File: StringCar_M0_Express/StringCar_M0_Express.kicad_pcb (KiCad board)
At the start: 2 copper layers, 50.8 x 22.9 mm, 48 parts, among them J1 USB_MICRO, J2 SENSOR_IN, J3 SWD, J4 STEMMA-QT, J5 MOTOR, J6 LIPO_BATT, Q1 DMG2305UX-13, Q2 DMG2305UX-13, SW1 RESET, SW2 POWER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

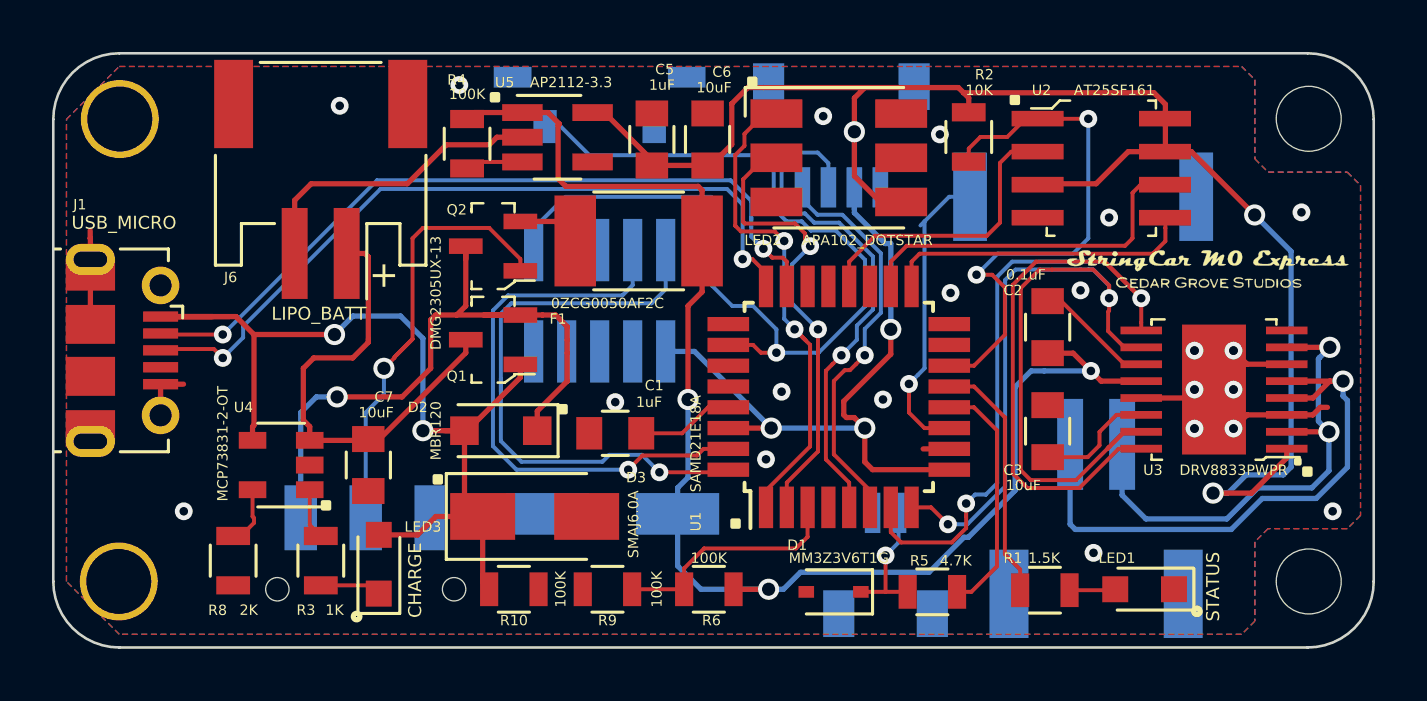
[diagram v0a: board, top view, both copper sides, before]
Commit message: update pcb layout and logo graphics
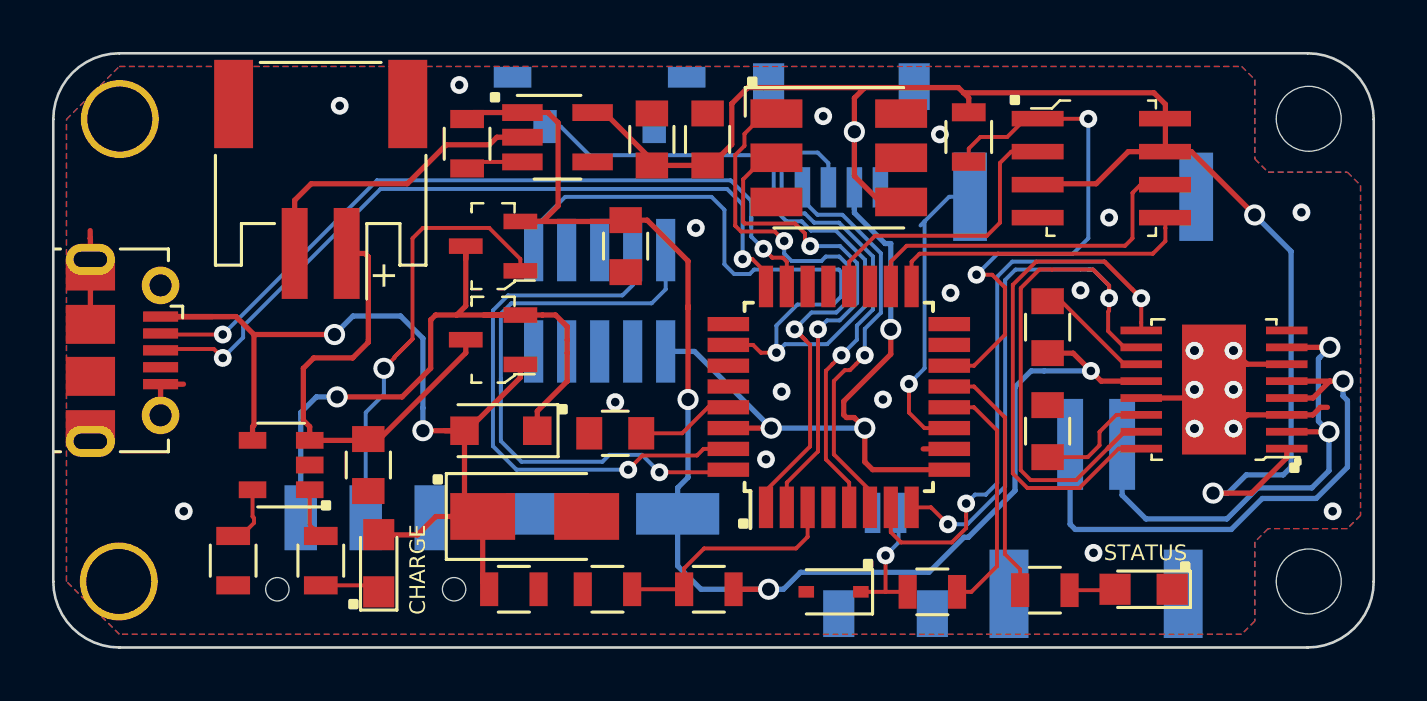
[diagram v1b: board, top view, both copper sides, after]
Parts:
- removed F1: 0ZCG0050AF2C, Resistors_SMD:R_1812
- removed the G*** at (138.4, 102.3)
- removed the G*** at (104.7, 97.0)
- removed the G*** at (105.3, 106.8)
- removed the G*** at (123.7, 103.1)
- removed the G*** at (124.3, 108.3)
- added C8: 0.01uF, Capacitors_SMD:C_0805, F.Cu at (116.0, 101.4)
- added G***: LOGO, Adafruit:stringcar_m0_express_6_5mmx2_8mm, B.Cu at (102.6, 97.6)
- added G***: LOGO, Adafruit:Blinka_3mmx3mm, F.Cu at (116.1, 105.3)
- added G***: LOGO, Adafruit:stringcar_m0_express_6_5mmx2_8mm, F.Cu at (140.5, 102.2)
- added G***: LOGO, Adafruit:Blinka_3mmx3mm, B.Cu at (98.2, 99.8)
- LED1, LED3: footprint Adafruit:D_0805_hand_soldering -> LEDs:LED_0805
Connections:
- Q2 pad 2: /Vsw -> /V+
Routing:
- net /~RESET: track 39.0 -> 44.1 mm
- net /DOTSTAR_DI: track 19.3 -> 22.9 mm
- net /Vsw: track 2.42 -> 0.00 mm
- net /DOTSTAR_CI: track 17.6 -> 19.2 mm
- net /V+: track 54.0 -> 55.3 mm
- net GND: vias 21 -> 22
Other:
- board text added: "--GND--"
- board text added: "2019-10-20 v04"
- board text added: "3V"
- board text added: "C"
- board text added: "D"
- board text added: "G 3V SDA SCL"
- board text added: "~R"
- board text removed: "+ CircuitPython compatible + AT-SAMD21E18A MPU + 2MByte flash RAM + Dual H-bridge motor controller + Sensor input + Stemma-QT connector (3V3) + On-board LiPo mgt 0.5A charge rate"
- board text removed: "2019-10-02 v03"
- board text removed: "3V3"
- board text removed: "GND"
- board text removed: "GND 3V3 SDA SCL"
- board text removed: "SWCLK"
- board text removed: "SWDIO"
- board text removed: "~RESET"
